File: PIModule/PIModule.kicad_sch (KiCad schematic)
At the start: 23 parts, among them J1 SigIn, J2 HVOut, J3 Heater, J4 HeaterOut, J5 HV, J6 SigOut, J7 NFB, J8 PresencePot, U1 ECC83

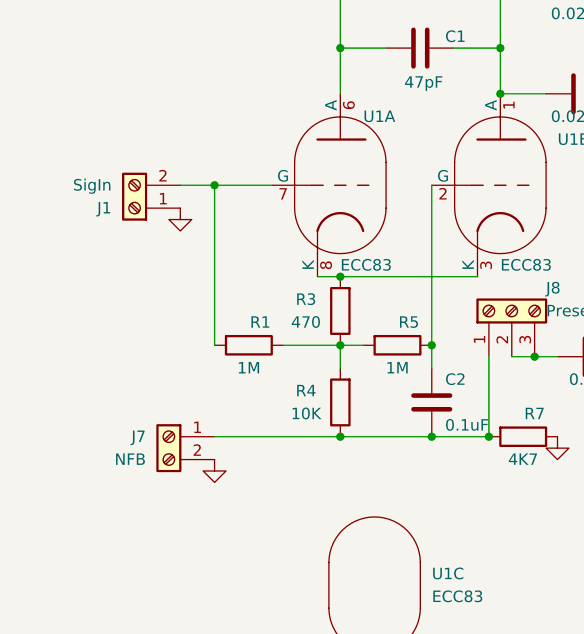
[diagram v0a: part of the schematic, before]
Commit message: Change connector footprints to contain 3D models. Make necessary PCB modifications to address errors found in the design
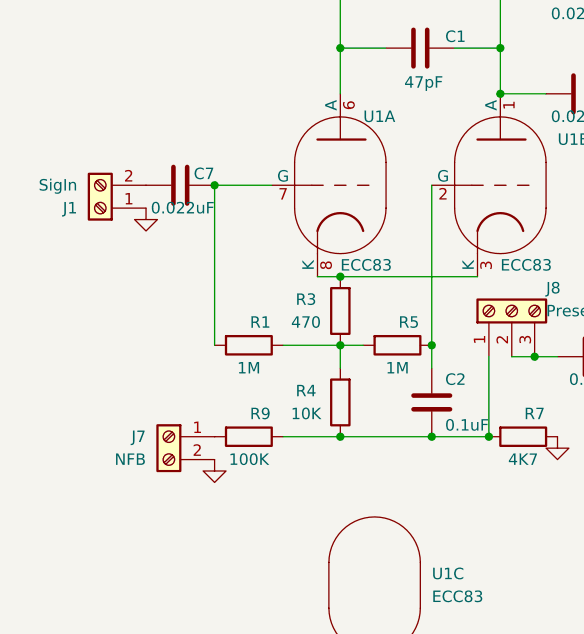
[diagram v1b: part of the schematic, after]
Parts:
- added C7: 0.022uF, Capacitor_THT:C_Rect_L13.0mm_W4.0mm_P10.00mm_FKS3_FKP3_MKS4, symbol Device:C
- added R9: 100K, Resistor_THT:R_Axial_DIN0309_L9.0mm_D3.2mm_P12.70mm_Horizontal, symbol Device:R
- C3, C4: footprint CustomFootprints:FG26 Cap -> Capacitor_THT:C_Rect_L13.0mm_W4.0mm_P10.00mm_FKS3_FKP3_MKS4
- J1, J2, J5: footprint Connector_Molex:Molex_Micro-Fit_3.0_43650-0200_1x02_P3.00mm_Horizontal -> CustomFootprints:Molex_Micro-Fit_3.0_43650-0200_1x02_P3.00mm_Horizontal
- J3, J4: footprint Connector_Molex:Molex_Micro-Fit_3.0_43650-0215_1x02_P3.00mm_Vertical -> CustomFootprints:Molex_Micro-Fit_3.0_43650-0215_1x02_P3.00mm_Vertical
- J6: footprint Connector_Molex:Molex_Micro-Fit_3.0_43650-0300_1x03_P3.00mm_Horizontal -> CustomFootprints:Molex_Micro-Fit_3.0_43650-0300_1x03_P3.00mm_Horizontal
- J7: footprint Connector_Molex:Molex_Micro-Fit_3.0_43650-0200_1x02_P3.00mm_Horizontal -> CustomFootprints:Molex_Micro-Fit_3.0_43650-0215_1x02_P3.00mm_Vertical
- J8: footprint Connector_Molex:Molex_Micro-Fit_3.0_43650-0315_1x03_P3.00mm_Vertical -> CustomFootprints:Molex_Micro-Fit_3.0_43650-0315_1x03_P3.00mm_Vertical
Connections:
- net at C2.1, J8.1 (Pin_1), R4.1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: now also R9.1; no longer J7.1 (Pin_1)
- net at R1.2, U1.7 (G): now also C7.2; no longer J1.2 (Pin_2)
- new net: C7.1, J1.2 (Pin_2)
- new net: J7.1 (Pin_1), R9.2
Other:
- moved on the sheet: J1
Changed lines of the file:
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@@
-    (stroke (width 0) (type default))
-  )
-  (wire (pts (xy 121.92 116.84) (xy 135.89 116.84))
     (stroke (width 0) (type default))
   )
@@
     (stroke (width 0) (type default))
   )
+  (wire (pts (xy 129.54 116.84) (xy 135.89 116.84))
+    (stroke (width 0) (type default))
+  )
   (wire (pts (xy 146.05 109.22) (xy 146.05 106.68))
     (stroke (width 0) (type default))
@@
   )
   (wire (pts (xy 133.35 99.06) (xy 135.89 99.06))
-    (stroke (width 0) (type default))
-  )
-  (wire (pts (xy 118.11 88.9) (xy 121.92 88.9))
     (stroke (width 0) (type default))
   )
@@
     )
   )
+  (symbol (lib_id "Device:C") (at 118.11 88.9 90) (unit 1)
+    (in_bom yes) (on_board yes) (dnp no)
+    (property "Reference" "C7" (at 121.92 87.63 90)
+      (effects (font (size 1.27 1.27)) (justify left))
+    )
+    (property "Value" "0.022uF" (at 121.92 91.44 90)
+      (effects (font (size 1.27 1.27)) (justify left))
+    )
+    (property "Footprint" "Capacitor_THT:C_Rect_L13.0mm_W4.0mm_P10.00mm_FKS3_FKP3_MKS4" (at 121.92 87.9348 0)
+      (effects (font (size 1.27 1.27)) hide)
+    )
+    (property "Datasheet" "~" (at 118.11 88.9 0)
+      (effects (font (size 1.27 1.27)) hide)
+    )
+    (pin "2")
+    (pin "1")
+    (instances
+      (project "PIModule"
+        (path "/d33a444a-501f-4cbb-9f48-c90ca4f3673f"
+          (reference "C7") (unit 1)
+        )
+      )
+    )
+  )
   (symbol (lib_id "power:HT") (at 153.67 57.15 0) (unit 1)
     (in_bom yes) (on_board yes) (dnp no)
@@
       (effects (font (size 1.27 1.27)) (justify left))
     )
-    (property "Footprint" "CustomFootprints:FG26 Cap" (at 166.37 65.0748 0)
+    (property "Footprint" "Capacitor_THT:C_Rect_L13.0mm_W4.0mm_P10.00mm_FKS3_FKP3_MKS4" (at 166.37 65.0748 0)
       (effects (font (size 1.27 1.27)) hide)
     )
@@
     )
   )
-  (symbol (lib_id "Connector:Screw_Terminal_01x02") (at 113.03 91.44 180) (unit 1)
-    (in_bom yes) (on_board yes) (dnp no)
-    (property "Reference" "J1" (at 110.49 91.44 0)
-      (effects (font (size 1.27 1.27)) (justify left))
-    )
-    (property "Value" "SigIn" (at 110.49 88.9 0)
-      (effects (font (size 1.27 1.27)) (justify left))
-    )
-    (property "Footprint" "Connector_Molex:Molex_Micro-Fit_3.0_43650-0200_1x02_P3.00mm_Horizontal" (at 113.03 91.44 0)
-      (effects (font (size 1.27 1.27)) hide)
-    )
-    (property "Datasheet" "~" (at 113.03 91.44 0)
+  (symbol (lib_id "Connector:Screw_Terminal_01x02") (at 109.22 91.44 180) (unit 1)
+    (in_bom yes) (on_board yes) (dnp no)
+    (property "Reference" "J1" (at 106.68 91.44 0)
+      (effects (font (size 1.27 1.27)) (justify left))
+    )
+    (property "Value" "SigIn" (at 106.68 88.9 0)
+      (effects (font (size 1.27 1.27)) (justify left))
+    )
+    (property "Footprint" "CustomFootprints:Molex_Micro-Fit_3.0_43650-0200_1x02_P3.00mm_Horizontal" (at 109.22 91.44 0)
+      (effects (font (size 1.27 1.27)) hide)
+    )
+    (property "Datasheet" "~" (at 109.22 91.44 0)
       (effects (font (size 1.27 1.27)) hide)
     )
@@
       (effects (font (size 1.27 1.27)) (justify left))
     )
-    (property "Footprint" "CustomFootprints:FG26 Cap" (at 166.37 77.7748 0)
+    (property "Footprint" "Capacitor_THT:C_Rect_L13.0mm_W4.0mm_P10.00mm_FKS3_FKP3_MKS4" (at 166.37 77.7748 0)
       (effects (font (size 1.27 1.27)) hide)
     )
@@
       (effects (font (size 1.27 1.27)) (justify left))
     )
-    (property "Footprint" "Connector_Molex:Molex_Micro-Fit_3.0_43650-0300_1x03_P3.00mm_Horizontal" (at 181.61 68.58 0)
+    (property "Footprint" "CustomFootprints:Molex_Micro-Fit_3.0_43650-0300_1x03_P3.00mm_Horizontal" (at 181.61 68.58 0)
       (effects (font (size 1.27 1.27)) hide)
     )
@@
       (effects (font (size 1.27 1.27)) (justify left))
     )
-    (property "Footprint" "Connector_Molex:Molex_Micro-Fit_3.0_43650-0215_1x02_P3.00mm_Vertical" (at 152.4 148.59 0)
+    (property "Footprint" "CustomFootprints:Molex_Micro-Fit_3.0_43650-0215_1x02_P3.00mm_Vertical" (at 152.4 148.59 0)
       (effects (font (size 1.27 1.27)) hide)
     )
@@
       (effects (font (size 1.27 1.27)) (justify left))
     )
-    (property "Footprint" "Connector_Molex:Molex_Micro-Fit_3.0_43650-0215_1x02_P3.00mm_Vertical" (at 127 146.05 0)
+    (property "Footprint" "CustomFootprints:Molex_Micro-Fit_3.0_43650-0215_1x02_P3.00mm_Vertical" (at 127 146.05 0)
       (effects (font (size 1.27 1.27)) hide)
     )
@@
       (effects (font (size 1.27 1.27)) (justify left))
     )
-    (property "Footprint" "Connector_Molex:Molex_Micro-Fit_3.0_43650-0200_1x02_P3.00mm_Horizontal" (at 160.02 39.37 0)
+    (property "Footprint" "CustomFootprints:Molex_Micro-Fit_3.0_43650-0200_1x02_P3.00mm_Horizontal" (at 160.02 39.37 0)
       (effects (font (size 1.27 1.27)) hide)
     )
@@
     )
   )
+  (symbol (lib_id "Device:R") (at 125.73 116.84 270) (unit 1)
+    (in_bom yes) (on_board yes) (dnp no)
+    (property "Reference" "R9" (at 127 114.3 90)
+      (effects (font (size 1.27 1.27)))
+    )
+    (property "Value" "100K" (at 125.73 119.38 90)
+      (effects (font (size 1.27 1.27)))
+    )
+    (property "Footprint" "Resistor_THT:R_Axial_DIN0309_L9.0mm_D3.2mm_P12.70mm_Horizontal" (at 125.73 115.062 90)
+      (effects (font (size 1.27 1.27)) hide)
+    )
+    (property "Datasheet" "~" (at 125.73 116.84 0)
+      (effects (font (size 1.27 1.27)) hide)
+    )
+    (pin "1")
+    (pin "2")
+    (instances
+      (project "PIModule"
+        (path "/d33a444a-501f-4cbb-9f48-c90ca4f3673f"
+          (reference "R9") (unit 1)
+        )
+      )
+    )
+  )
   (symbol (lib_id "Device:R") (at 156.21 116.84 270) (unit 1)
     (in_bom yes) (on_board yes) (dnp no)
@@
     )
   )
-  (symbol (lib_id "power:GND") (at 118.11 91.44 0) (unit 1)
+  (symbol (lib_id "power:GND") (at 114.3 91.44 0) (unit 1)
     (in_bom yes) (on_board yes) (dnp no) (fields_autoplaced)
-    (property "Reference" "#PWR011" (at 118.11 97.79 0)
-      (effects (font (size 1.27 1.27)) hide)
-    )
-    (property "Value" "GND" (at 118.11 95.25 90)
+    (property "Reference" "#PWR011" (at 114.3 97.79 0)
+      (effects (font (size 1.27 1.27)) hide)
+    )
+    (property "Value" "GND" (at 114.3 95.25 90)
       (effects (font (size 1.27 1.27)) (justify right) hide)
     )
-    (property "Footprint" "" (at 118.11 91.44 0)
-      (effects (font (size 1.27 1.27)) hide)
-    )
-    (property "Datasheet" "" (at 118.11 91.44 0)
+    (property "Footprint" "" (at 114.3 91.44 0)
+      (effects (font (size 1.27 1.27)) hide)
+    )
+    (property "Datasheet" "" (at 114.3 91.44 0)
       (effects (font (size 1.27 1.27)) hide)
     )
@@
       (effects (font (size 1.27 1.27)) (justify left))
     )
-    (property "Footprint" "Connector_Molex:Molex_Micro-Fit_3.0_43650-0200_1x02_P3.00mm_Horizontal" (at 130.81 36.83 0)
+    (property "Footprint" "CustomFootprints:Molex_Micro-Fit_3.0_43650-0200_1x02_P3.00mm_Horizontal" (at 130.81 36.83 0)
       (effects (font (size 1.27 1.27)) hide)
     )
@@
       (effects (font (size 1.27 1.27)) (justify left))
     )
-    (property "Footprint" "Connector_Molex:Molex_Micro-Fit_3.0_43650-0200_1x02_P3.00mm_Horizontal" (at 116.84 116.84 0)
+    (property "Footprint" "CustomFootprints:Molex_Micro-Fit_3.0_43650-0215_1x02_P3.00mm_Vertical" (at 116.84 116.84 0)
       (effects (font (size 1.27 1.27)) hide)
     )
@@
       (effects (font (size 1.27 1.27)) (justify right))
     )
-    (property "Footprint" "Connector_Molex:Molex_Micro-Fit_3.0_43650-0315_1x03_P3.00mm_Vertical" (at 154.94 102.87 0)
-      (effects (font (size 1.27 1.27)) hide)
-    )
+    (property "Footprint" "CustomFootprints:Molex_Micro-Fit_3.0_43650-0315_1x03_P3.00mm_Vertical" (at 154.94 102.87 0)
+      (effects (font (size 1.27 1.27)) hide)
+    )
